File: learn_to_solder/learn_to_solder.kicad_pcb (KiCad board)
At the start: 2 copper layers, 83.2 x 47 mm, 8 parts, among them Q1 2N3904

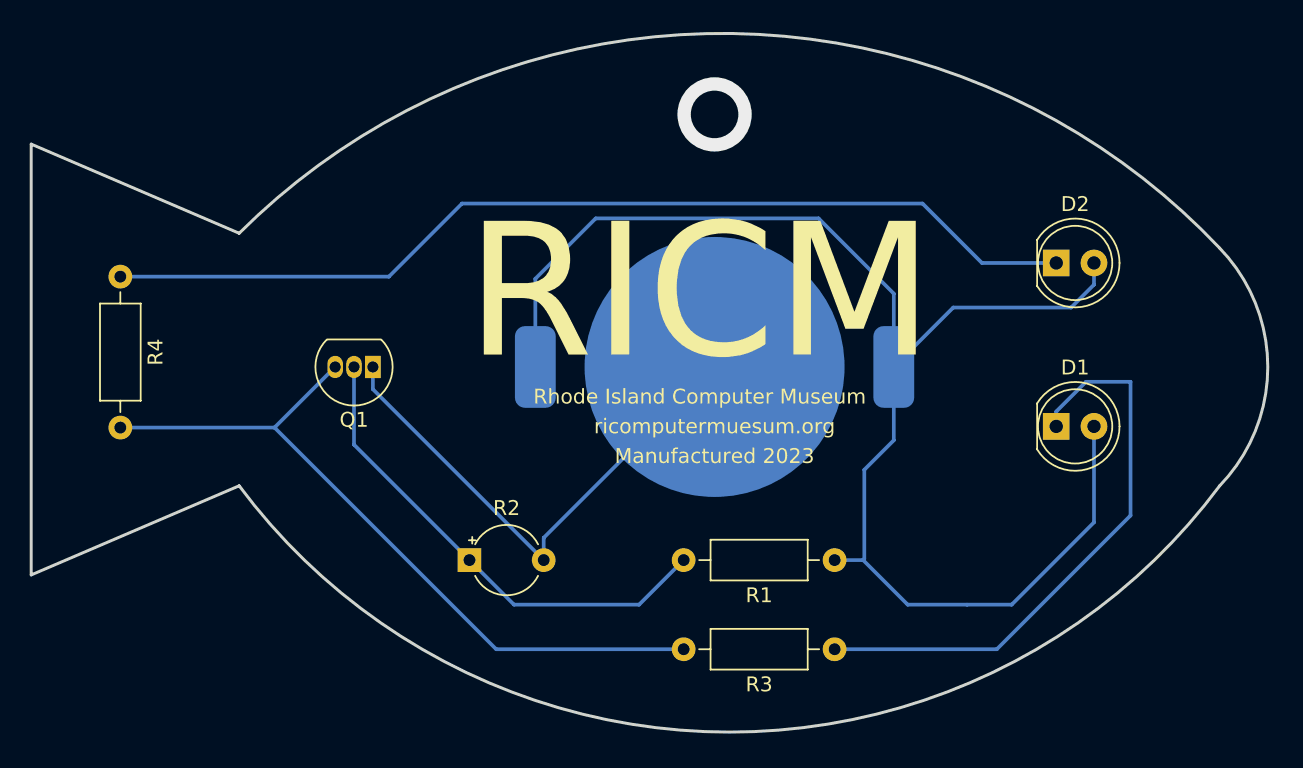
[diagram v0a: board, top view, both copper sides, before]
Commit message: Updated readme and silkscreen
Updated readme to correctly reflect kit components. Added labels in front silkscreen with resistor values to make assembly easier. Rearranged resistors to put both 220s next to each other.
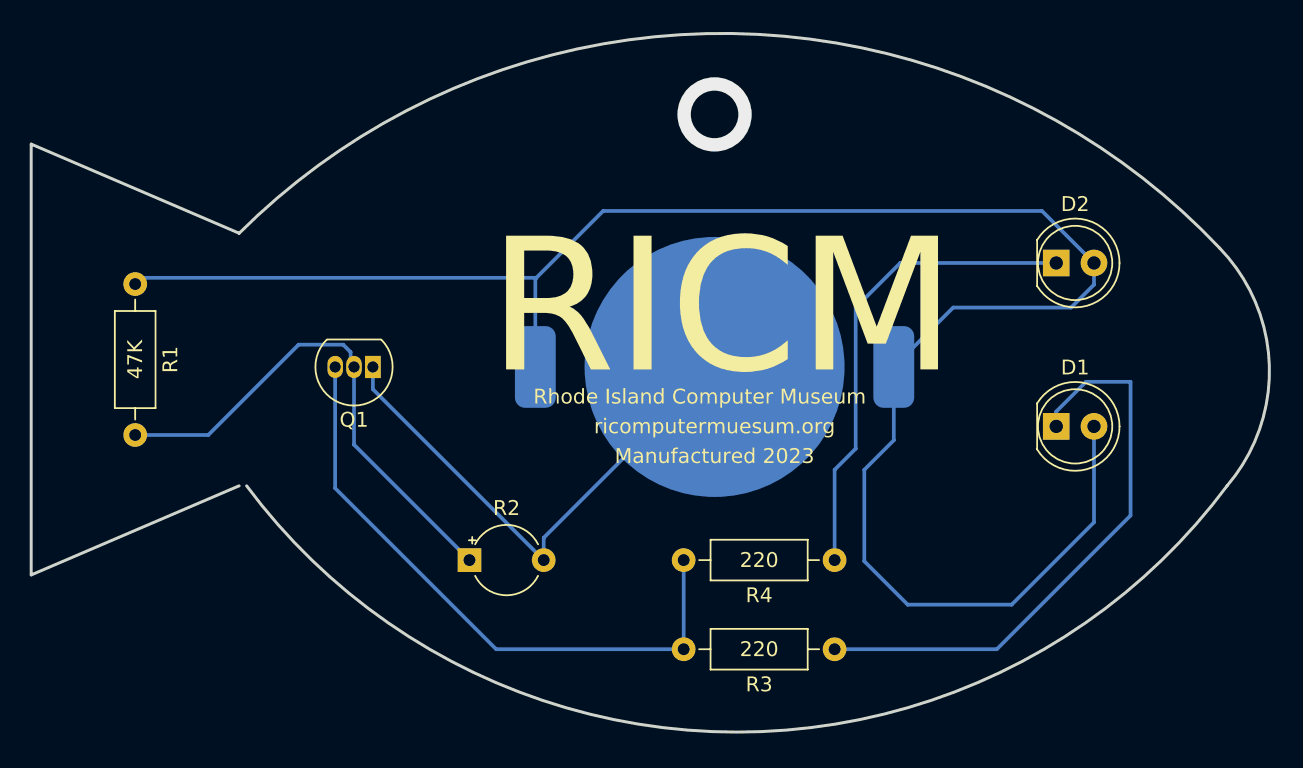
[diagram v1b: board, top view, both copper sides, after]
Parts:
- moved R4 51.7 mm to (138.1, 89.0), turned to 180 degrees
- moved R1 50.6 mm to (91.0, 70.4), turned to -90 degrees
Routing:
- net Net-(D2-Pad1): track 66.7 -> 32.3 mm
- net Net-(BT1-Pad1): track 97.3 -> 130.6 mm
- net Net-(Q1-Pad3): track 49.9 -> 42.0 mm
- net Net-(Q1-Pad2): track 33.1 -> 34.4 mm
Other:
- board size 83.2 x 47 mm -> 83.3 x 47 mm
- board text added: "220"
- board text added: "47K"

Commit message: V2 updates
Rearranged resistors to group both 220s together. Added slide switch to turn off without removing battery. Corrected typos in silkscreen. Fixed clip slot size.
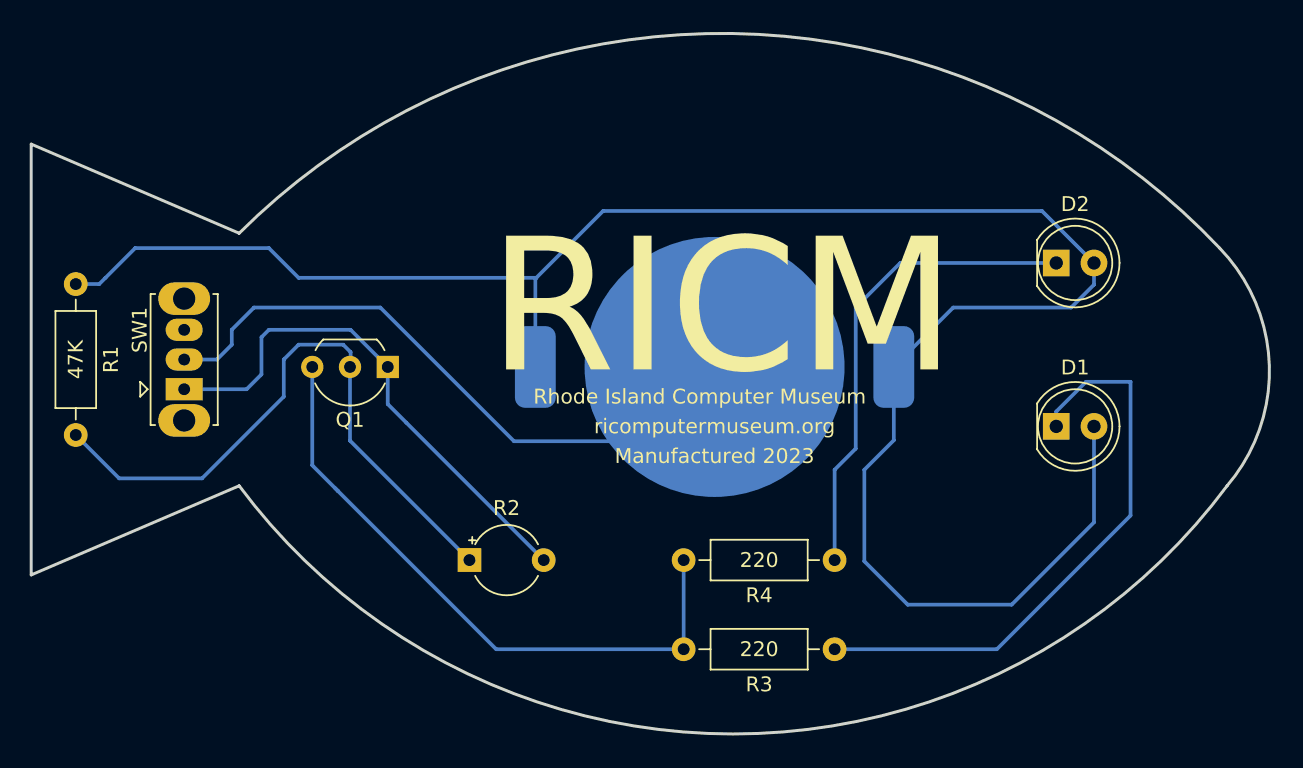
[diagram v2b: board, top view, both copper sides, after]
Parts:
- added SW1: SW_SPDT, Button_Switch_THT:SW_Slide_1P2T_CK_OS102011MS2Q, F.Cu at (94.3, 77.5)
- Q1: footprint Package_TO_SOT_THT:TO-92_Inline -> Package_TO_SOT_THT:TO-92_Inline_Wide
- R1: value R -> 47K
- R3, R4: value R -> 220
- moved R1 4.00 mm to (87.0, 70.4)
- moved Q1 1.00 mm to (108.0, 76.0)
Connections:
- BT1 pad 2: GND -> Net-(BT1-Pad2)
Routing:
- net Net-(BT1-Pad2): track 0.00 -> 43.5 mm
- net Net-(Q1-Pad2): track 34.4 -> 42.4 mm
- net Net-(BT1-Pad1): track 130.6 -> 136.3 mm
- net Net-(Q1-Pad3): track 42.0 -> 42.9 mm
- net (no net): vias 1 -> 0
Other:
- board size 83.3 x 47 mm -> 83.3 x 47.2 mm
- board text added: "ricomputermuseum.org"
- board text removed: "ricomputermuesum.org"

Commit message: v3 edits
Filleted sharp board edge. Added slot footprint for hanger.
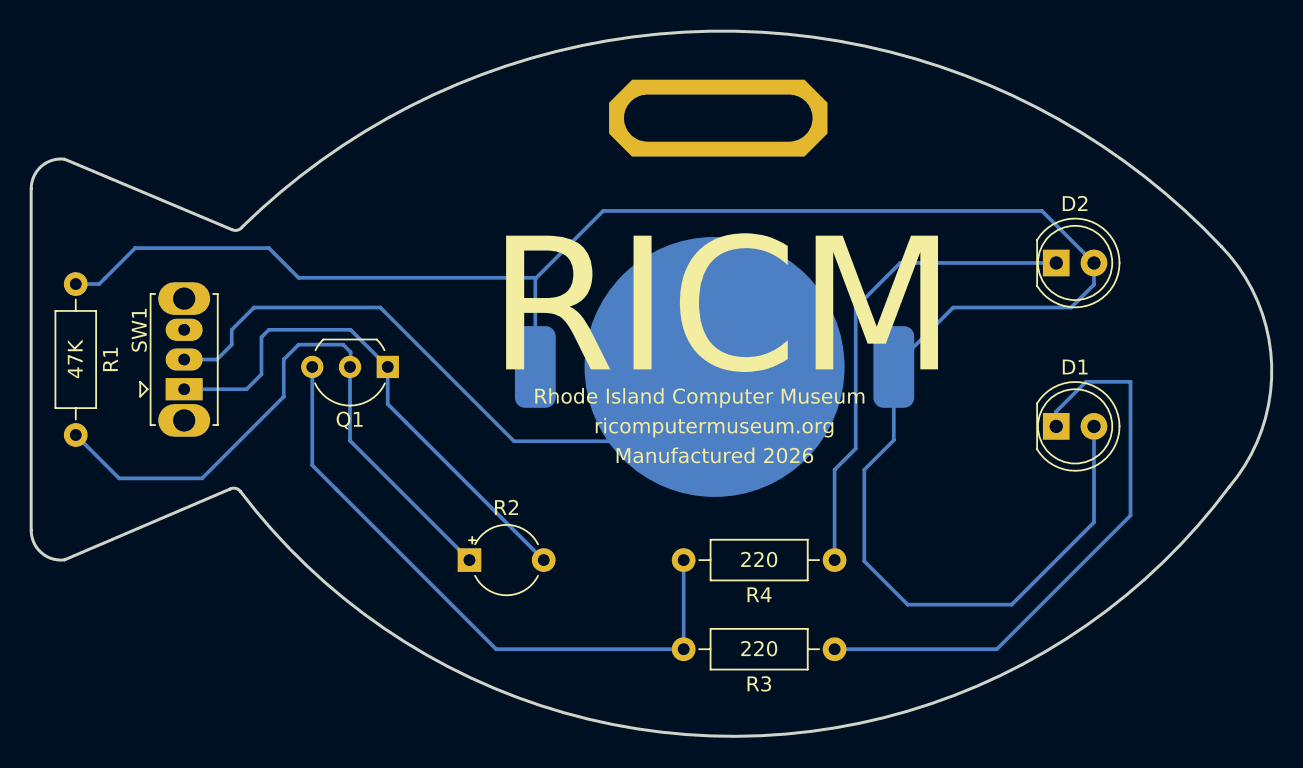
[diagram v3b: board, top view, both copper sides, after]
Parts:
- added REF**: MountingHole_2.5mm_Pad_TopBottom, MountingHole:MountingHole_2.5mm_Pad_TopBottom, F.Cu at (130.2, 59.2)
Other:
- board size 83.3 x 47.2 mm -> 83.5 x 47.5 mm
- board text added: "Manufactured 2026"
- board text removed: "Manufactured 2023"
